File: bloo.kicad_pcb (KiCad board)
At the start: 2 copper layers, 86 x 99 mm, 103 parts, among them J1 Serial Debug Header, J10 Conn_01x06_Female, J2 SWD Header, J4 Conn_ARM_JTAG_SWD_10, J5 SWD Header, M1 M1_Conn_Alt, M2 M2_Conn_Alt, Q0 TEFT4300, Q1 TEFT4300, Q10 Q_NMOS_GSD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

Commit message: updated PCB
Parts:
- moved TP2 81.5 mm to (112.8, 117.4)
- moved TP4 13.4 mm to (194.0, 122.4)
- moved C10 3.29 mm to (156.4, 121.1)
- moved U4 2.97 mm to (183.1, 115.3)
- moved C25 2.80 mm to (187.7, 122.3), turned to -90 degrees
- moved U5 2.78 mm to (178.8, 120.3)
- moved U6 2.46 mm to (178.8, 115.7)
- moved C11 2.40 mm to (188.5, 113.7)
- moved C12 2.38 mm to (188.9, 116.7)
- moved L1 2.12 mm to (183.0, 123.2)
- moved C16 1.86 mm to (152.3, 117.8), turned to 180 degrees
- moved MOS1 1.26 mm to (174.1, 115.0)
- moved C1 1.19 mm to (176.5, 110.9)
- moved C9 1.10 mm to (171.0, 110.8)
- moved S1 1.05 mm to (175.3, 100.9)
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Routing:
- net +5V_NET: track 51.2 -> 59.5 mm
- net +5V: track 302.8 -> 308.3 mm
- net +3V3: track 446.6 -> 450.8 mm
- net GND: track 34.2 -> 38.1 mm
- net RST: track 170.3 -> 172.9 mm
- net Net-(S1-Pad3): track 11.4 -> 13.2 mm
- net M1_SPD: track 89.5 -> 87.8 mm
- net 3V3_BYP: track 11.1 -> 9.43 mm
- net M1_OUT_2: track 46.0 -> 47.5 mm
- net LED_GREEN: track 27.6 -> 26.5 mm
- net +3.3VA: track 200.6 -> 199.6 mm
- net BUTTON_3: track 40.6 -> 39.5 mm
- net EMIT_4: track 36.1 -> 37.0 mm
- net Net-(BT1-+): track 15.0 -> 15.8 mm
- net USART1_RX: track 25.7 -> 26.3 mm
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
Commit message: finished pcb
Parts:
- added G***: LOGO, LOGO, B.Cu at (153.9, 138.3)
- moved R11 9.70 mm to (143.2, 150.9), turned to -90 degrees
- moved R9 2.22 mm to (139.2, 150.9), turned to -90 degrees
- moved C17 0.74 mm to (186.4, 107.7)
- moved C15 0.30 mm to (157.8, 188.2)
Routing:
- net +3V3: track 450.8 -> 421.1 mm
- net +5V_NET: track 59.5 -> 64.8 mm
- net BUTTON_2: track 25.6 -> 27.3 mm
- net EMIT_1: track 39.7 -> 41.2 mm
- net SWDIO: track 80.7 -> 81.8 mm
- net BUTTON: track 55.2 -> 56.2 mm
- net BUTTON_3: track 39.5 -> 38.7 mm, vias 3 -> 2
- net M1_OUT_2: track 47.5 -> 48.1 mm
- net M1_OUT_1: track 52.5 -> 53.0 mm
- net GND: vias 27 -> 33
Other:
- board text added: "+3V3"
- board text added: "+5V_NET"
- board text added: "BAT_NET"
- board text added: "BLE_STATE --"
- board text added: "BT1+"
- board text added: "GND"
- board text added: "Jonathan Lin UCI IEEE Micromouse 2025 - 2026"
- board text added: "VCC"
- board text added: "V_EXT_TP"
- board text added: "V_METER"
- board text added: "| | GND"
- board text added: "| | VCC"
- board text added: "／＞ フ | _ _| ／` ミ＿xノ / | / ヽ ﾉ │ | | | ／￣| | | | (￣ヽ＿_ヽ_)__) ＼二)"

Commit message: eaton's edits
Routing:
- net +3.3VA: track 199.4 -> 185.1 mm
- net GND: track 38.1 -> 27.1 mm, vias 33 -> 26
- net BATT_NET: track 45.7 -> 38.9 mm
- net +5V: track 307.9 -> 313.4 mm
- net +3V3: track 421.1 -> 416.4 mm
- net 3V3_BYP: track 9.43 -> 7.37 mm

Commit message: final final revision of micromouse pcb
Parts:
- moved Q1 1.15 mm to (156.9, 195.3), turned to 55 degrees
- moved Q3 0.97 mm to (148.8, 193.2), turned to -55 degrees
- moved D3 0.88 mm to (142.2, 191.9), turned to -55 degrees
- moved D1 0.88 mm to (163.0, 193.9), turned to 55 degrees
- moved R14 0.85 mm to (172.7, 194.6), turned to 135 degrees
- moved R16 0.65 mm to (132.7, 194.7)
- moved M_MH1 0.59 mm to (152.4, 140.0)
- moved M_MH2 0.57 mm to (154.4, 139.9)
- moved R6 0.52 mm to (168.1, 190.6)
- moved Q12 0.38 mm to (135.5, 192.6)
- moved G*** 0.31 mm to (153.6, 138.5)
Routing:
- net GND: track 27.1 -> 10.6 mm, vias 26 -> 14
- net +3.3VA: track 185.1 -> 188.6 mm
- net RECEIV_3: track 27.0 -> 29.6 mm
- net EMIT_2: track 26.8 -> 25.0 mm
- net +5V: track 313.4 -> 311.7 mm
- net Net-(D1-K): track 6.59 -> 7.13 mm
- net AGND: track 159.8 -> 159.4 mm, vias 7 -> 6
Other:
- board size 86 x 99 mm -> 86 x 99.2 mm
- board text removed: "／＞ フ | _ _| ／` ミ＿xノ / | / ヽ ﾉ │ | | | ／￣| | | | (￣ヽ＿_ヽ_)__) ＼二)"

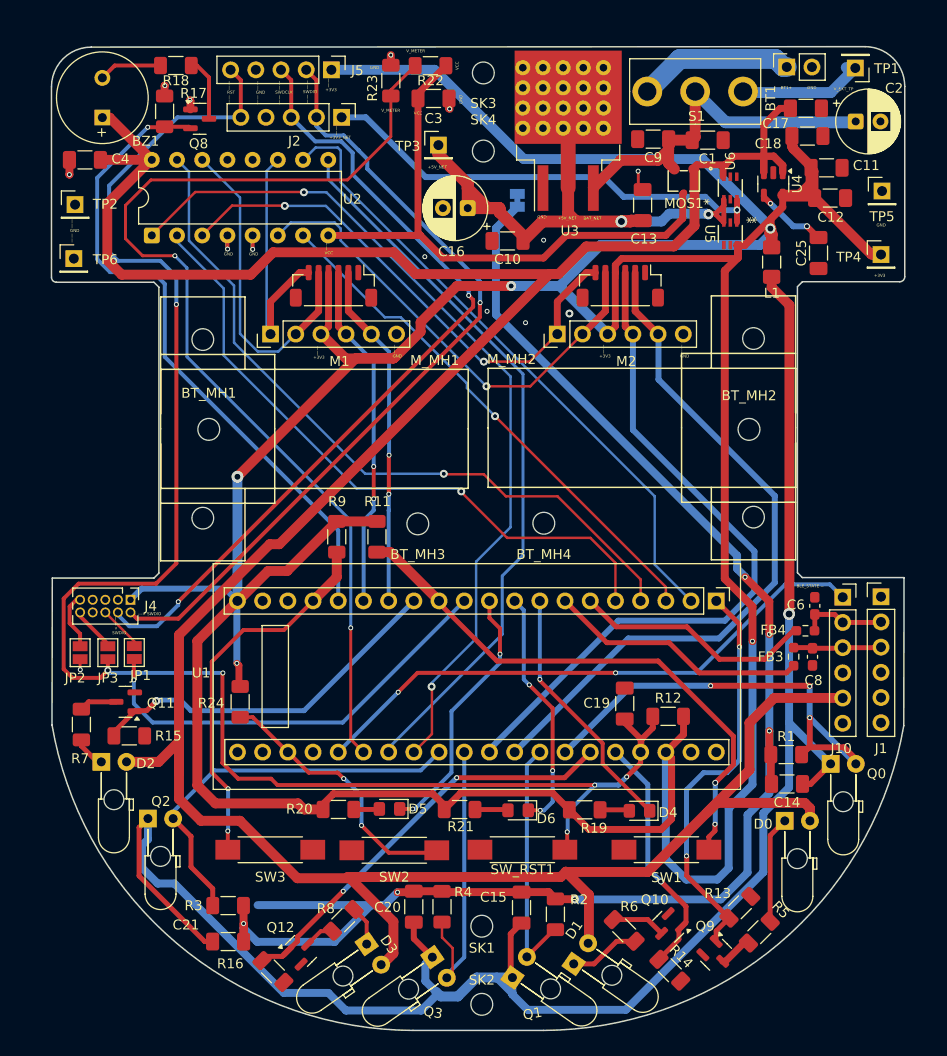
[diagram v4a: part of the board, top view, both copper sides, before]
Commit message: revised trace widths
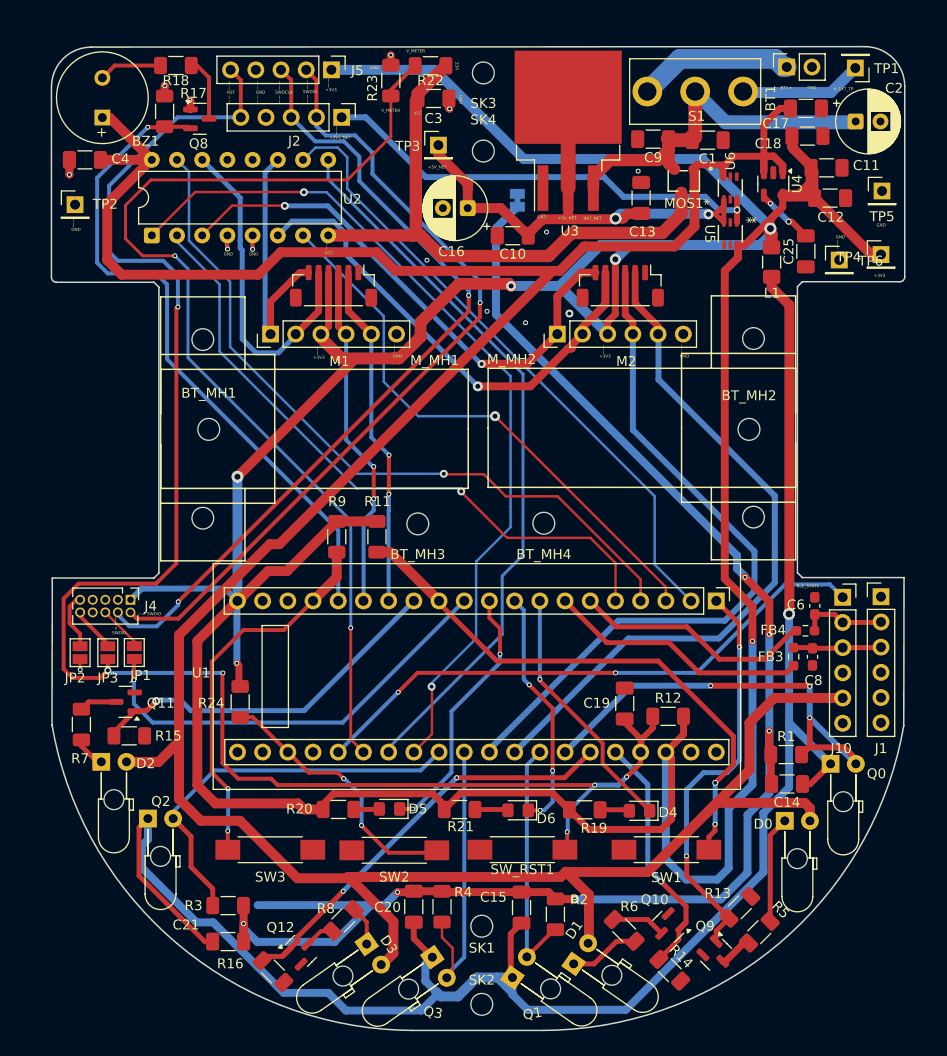
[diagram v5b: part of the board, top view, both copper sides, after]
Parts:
- moved TP6 77.1 mm to (189.8, 123.0)
- moved C25 1.29 mm to (186.4, 122.1)
- moved C10 0.75 mm to (156.9, 120.5)
- moved C13 0.74 mm to (169.8, 116.7)
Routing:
- net +5V_NET: track 64.8 -> 56.3 mm
- net +3V3: track 416.4 -> 420.3 mm, vias 5 -> 6
- net M1_BACK: track 52.9 -> 56.5 mm
- net 3V3_BYP: track 7.37 -> 6.07 mm
- net GND: track 10.6 -> 9.44 mm
- net +5V: track 311.7 -> 310.5 mm
- net Net-(S1-Pad3): track 13.2 -> 12.3 mm
- net M1_OUT_2: track 48.1 -> 49.0 mm
- net M1_OUT_1: track 53.0 -> 53.8 mm
- net VCC: track 59.3 -> 58.6 mm
- net SWDIO: track 81.4 -> 82.0 mm
- net BATT_NET: track 38.9 -> 39.5 mm
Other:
- board text added: "GND | |"
